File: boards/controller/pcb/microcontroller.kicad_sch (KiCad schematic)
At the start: 23 parts, among them J1001 Conn_01x15_Socket, J1002 Conn_01x11_Socket, J1003 Conn_01x08_Socket, SW1001 SW_Push, SW1002 SW_Push, U1001 STM32U575RITx, X1001 16MHz

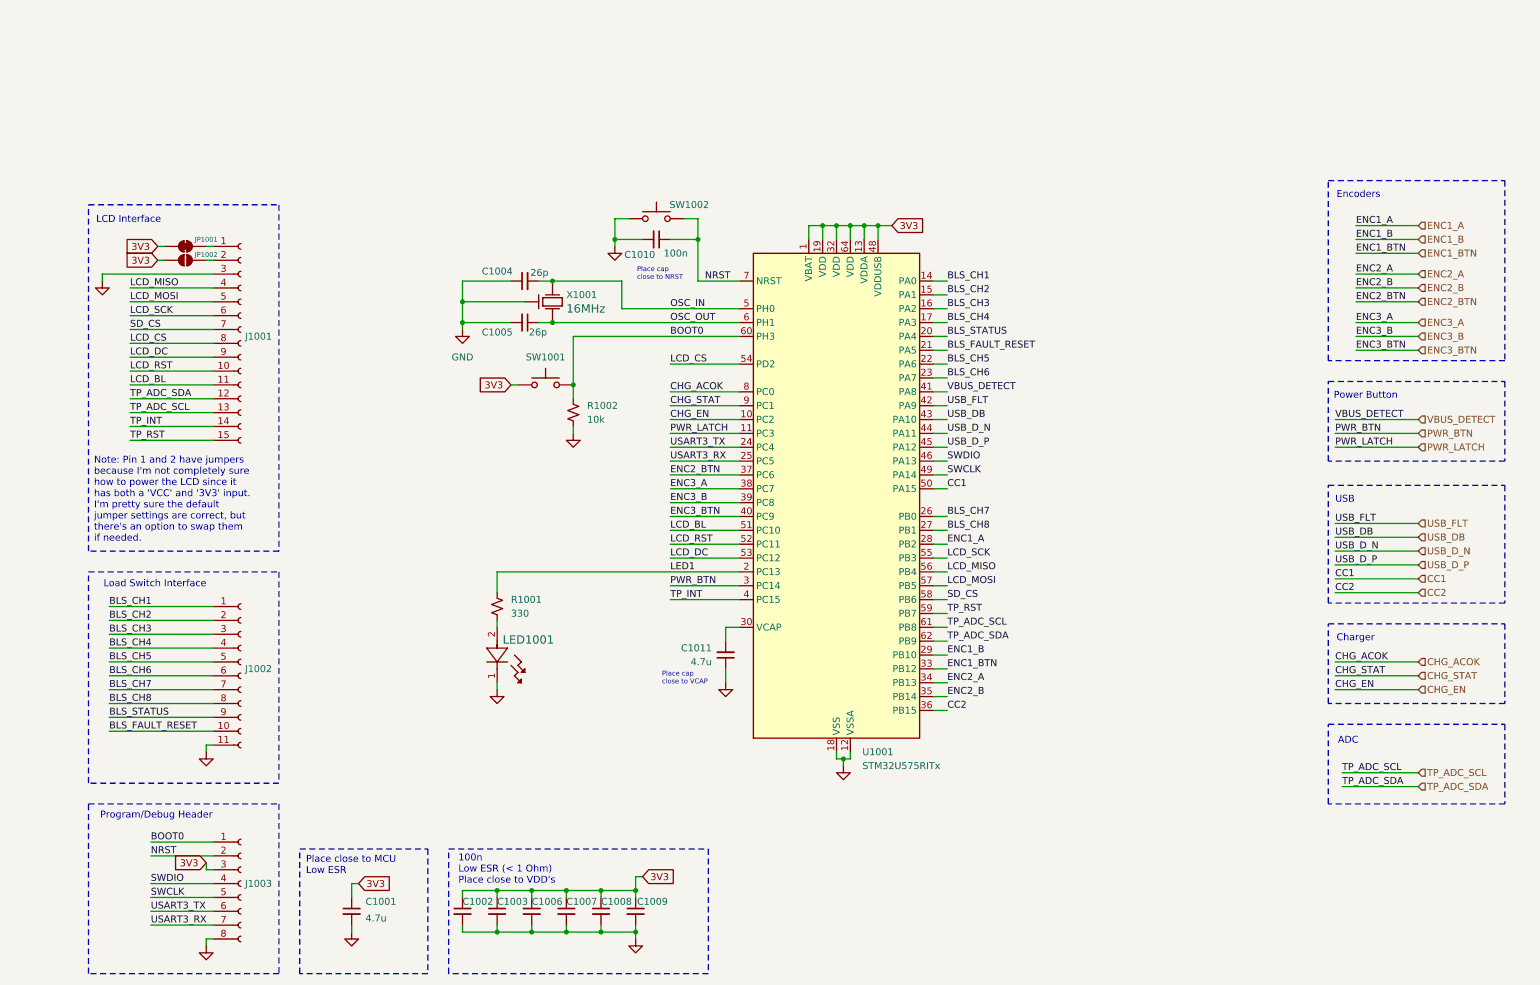
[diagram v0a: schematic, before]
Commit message: controller: pcb: Update schematic
Signed-off-by: Nicholas Loehrke <nicholasnloehrke@gmail.com>
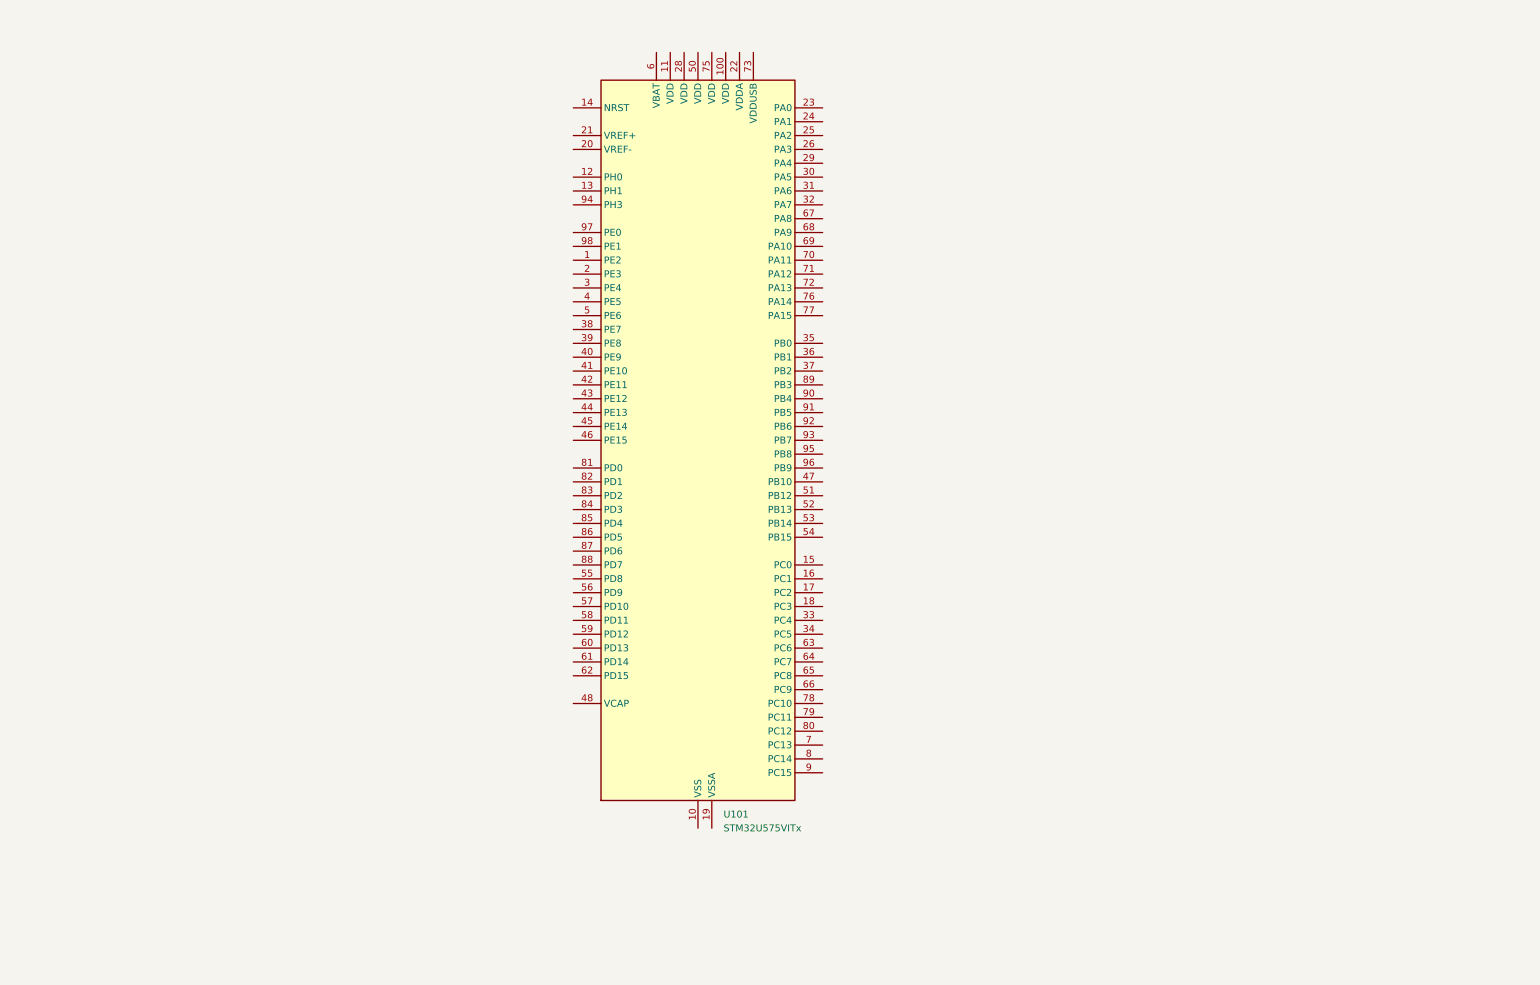
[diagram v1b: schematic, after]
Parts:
- removed C1001, C1011: 4.7u, symbol Device:C_Small
- removed C1002, C1003, C1006, C1007, C1008, C1009, C1010: 100n, symbol Device:C_Small
- removed C1004, C1005: 26p, symbol Device:C_Small
- removed J1001: Conn_01x15_Socket, symbol Connector:Conn_01x15_Socket
- removed J1002: Conn_01x11_Socket, symbol Connector:Conn_01x11_Socket
- removed J1003: Conn_01x08_Socket, symbol Connector:Conn_01x08_Socket
- removed JP1001: SolderJumper_2_Bridged, symbol Jumper:SolderJumper_2_Bridged
- removed JP1002: SolderJumper_2_Open, symbol Jumper:SolderJumper_2_Open
- removed LED1001: B1911PG--20D000514U1930, LED_B1911PG--20D000514U1930_HVK, symbol B1911PG__20D000514U1930:B1911PG--20D000514U1930
- removed R1001: 330, symbol Device:R_Small_US
- removed R1002: 10k, symbol Device:R_Small_US
- removed SW1001, SW1002: SW_Push, symbol Switch:SW_Push
- removed U1001: STM32U575RITx, Package_QFP:LQFP-64_10x10mm_P0.5mm, symbol MCU_ST_STM32U5:STM32U575RITx
- removed X1001: 16MHz, RH100-16.000-18-2030-EXT-TR_RAL, symbol RH100-16.000-18-2030-EXT-TR:RH100-16.000-18-2030-EXT-TR
- added U101: STM32U575VITx, Package_QFP:LQFP-100_14x14mm_P0.5mm, symbol MCU_ST_STM32U5:STM32U575VITx
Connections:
- new net: U101.10 (VSS), U101.27 (VSS), U101.49 (VSS), U101.74 (VSS), U101.99 (VSS)
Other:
- note removed: "100n Low ESR (< 1 Ohm) Place close to VDD's"
- note removed: "ADC"
- note removed: "Charger"
- note removed: "Encoders"
- note removed: "LCD Interface"
- note removed: "Load Switch Interface"
- note removed: "Note: Pin 1 and 2 have jumpers because I'm not completely sure how to power the LCD since it has both a 'VCC' and '3V3' input. I'm pretty sure the default jumper settings are correct, but there's an option to swap them if needed."
- note removed: "Place cap close to NRST"
- note removed: "Place cap close to VCAP"
- note removed: "Place close to MCU Low ESR"
- note removed: "Power Button"
- note removed: "Program/Debug Header"
- note removed: "USB"

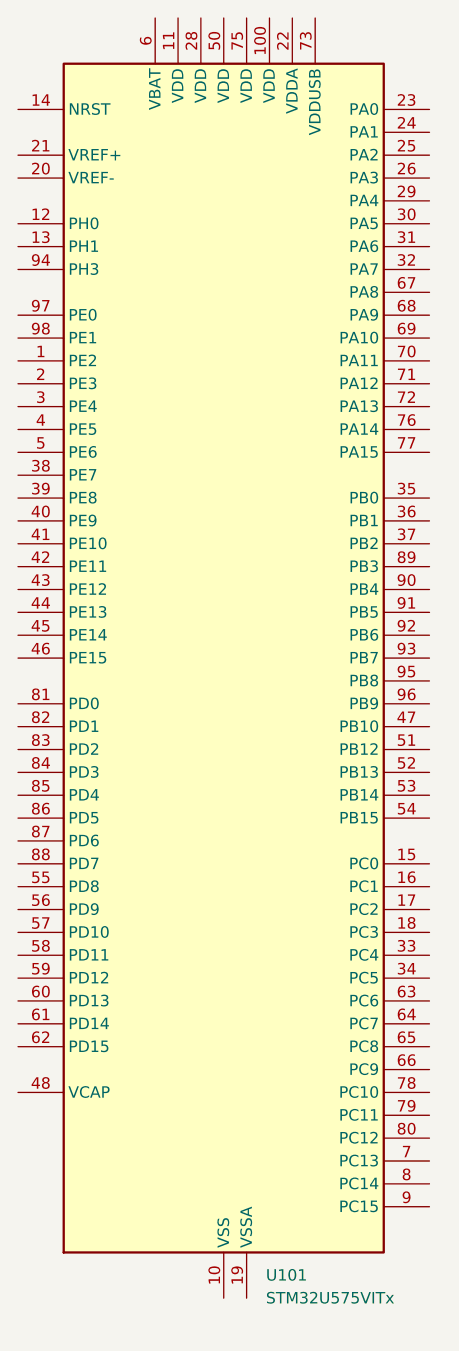
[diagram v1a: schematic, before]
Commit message: controller: pcb: Update schematic
Signed-off-by: Nicholas Loehrke <nicholasnloehrke@gmail.com>
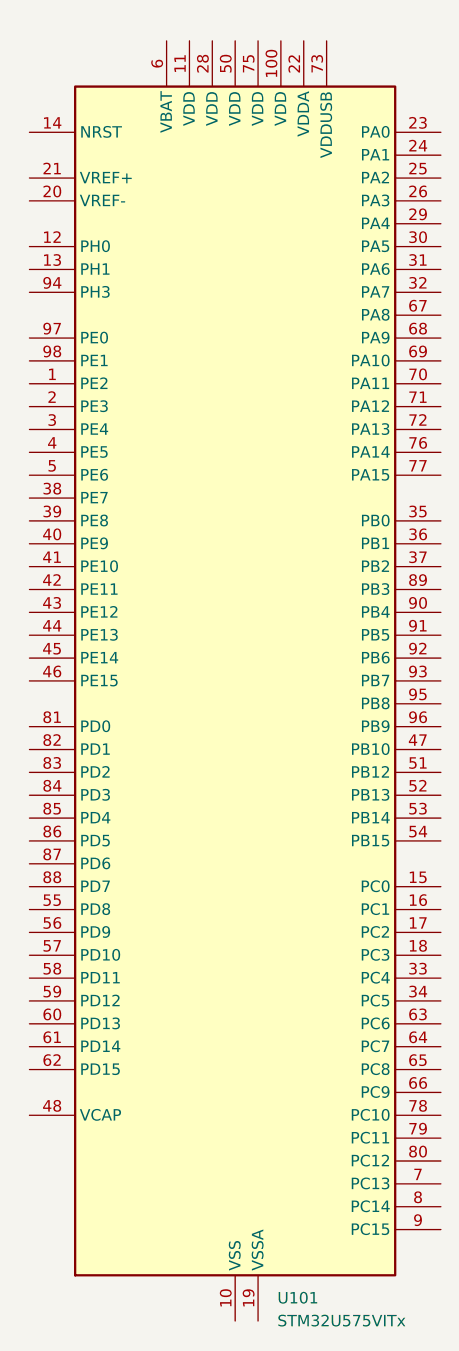
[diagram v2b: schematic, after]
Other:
- moved on the sheet: U101
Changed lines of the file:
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@@
 	(symbol
 		(lib_id "MCU_ST_STM32U5:STM32U575VITx")
-		(at 130.81 92.71 0)
+		(at 132.08 95.25 0)
 		(unit 1)
 		(exclude_from_sim no)
@@
 		(fields_autoplaced yes)
 		(property "Reference" "U101"
-			(at 135.4933 161.29 0)
+			(at 136.7633 163.83 0)
 			(effects
 				(font
@@
 		)
 		(property "Value" "STM32U575VITx"
-			(at 135.4933 163.83 0)
+			(at 136.7633 166.37 0)
 			(effects
 				(font
@@
 		)
 		(property "Footprint" "Package_QFP:LQFP-100_14x14mm_P0.5mm"
-			(at 113.03 158.75 0)
+			(at 114.3 161.29 0)
 			(effects
 				(font
@@
 		)
 		(property "Datasheet" "https://www.st.com/resource/en/datasheet/stm32u575vi.pdf"
-			(at 130.81 92.71 0)
+			(at 132.08 95.25 0)
 			(effects
 				(font
@@
 		)
 		(property "Description" "STMicroelectronics Arm Cortex-M33 MCU, 2048KB flash, 786KB RAM, 160 MHz, 1.71-3.6V, 82 GPIO, LQFP100"
-			(at 130.81 92.71 0)
+			(at 132.08 95.25 0)
 			(effects
 				(font

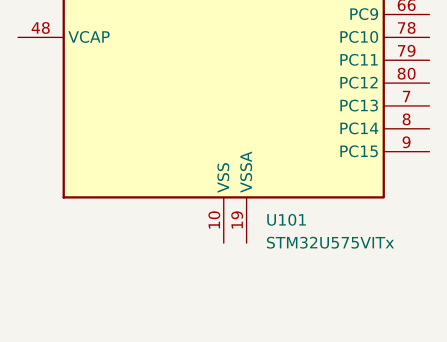
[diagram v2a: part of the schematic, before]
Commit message: controller: pcb: Update schematic
Signed-off-by: Nicholas Loehrke <nicholasnloehrke@gmail.com>
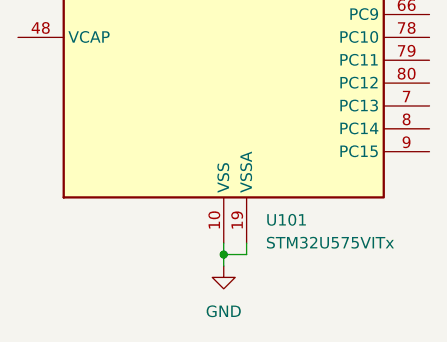
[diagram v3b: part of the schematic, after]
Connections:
- net GND: now reaches U101.10 (VSS), U101.27 (VSS), U101.49 (VSS), U101.74 (VSS), U101.99 (VSS)
- net GND: now also U101.19 (VSSA)
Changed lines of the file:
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@@
 	(generator_version "9.0")
 	(paper "A4")
+	(junction
+		(at 132.08 167.64)
+		(diameter 0)
+		(color 0 0 0 0)
+	)
+	(wire
+		(pts
+			(xy 134.62 166.37) (xy 134.62 167.64)
+		)
+		(stroke
+			(width 0)
+			(type default)
+		)
+	)
+	(wire
+		(pts
+			(xy 132.08 166.37) (xy 132.08 167.64)
+		)
+		(stroke
+			(width 0)
+			(type default)
+		)
+	)
+	(wire
+		(pts
+			(xy 132.08 167.64) (xy 132.08 168.91)
+		)
+		(stroke
+			(width 0)
+			(type default)
+		)
+	)
+	(wire
+		(pts
+			(xy 134.62 167.64) (xy 132.08 167.64)
+		)
+		(stroke
+			(width 0)
+			(type default)
+		)
+	)
 	(symbol
 		(lib_id "MCU_ST_STM32U5:STM32U575VITx")
@@
 					(unit 1)
 				)
+			)
+		)
+	)
+	(symbol
+		(lib_id "power:GND")
+		(at 132.08 168.91 0)
+		(unit 1)
+		(exclude_from_sim no)
+		(in_bom yes)
+		(on_board yes)
+		(dnp no)
+		(fields_autoplaced yes)
+		(property "Reference" "#PWR0301"
+			(at 132.08 175.26 0)
+			(effects
+				(font
+					(size 1.27 1.27)
+				)
+				(hide yes)
+			)
+		)
+		(property "Value" "GND"
+			(at 132.08 173.99 0)
+			(effects
+				(font
+					(size 1.27 1.27)
+				)
+			)
+		)
+		(property "Footprint" ""
+			(at 132.08 168.91 0)
+			(effects
+				(font
+					(size 1.27 1.27)
+				)
+				(hide yes)
+			)
+		)
+		(property "Datasheet" ""
+			(at 132.08 168.91 0)
+			(effects
+				(font
+					(size 1.27 1.27)
+				)
+				(hide yes)
+			)
+		)
+		(property "Description" "Power symbol creates a global label with name \"GND\" , ground"
+			(at 132.08 168.91 0)
+			(effects
+				(font
+					(size 1.27 1.27)
+				)
+				(hide yes)
+			)
+		)
+		(pin "1"
+		)
+		(instances
+			(project ""
+				(path "/5caba13a-97ae-46d4-856f-900b12012fd8/656fb25c-ff6c-44f4-9a62-a4f6fe4240ec"
+					(reference "#PWR0301")
+					(unit 1)
+				)

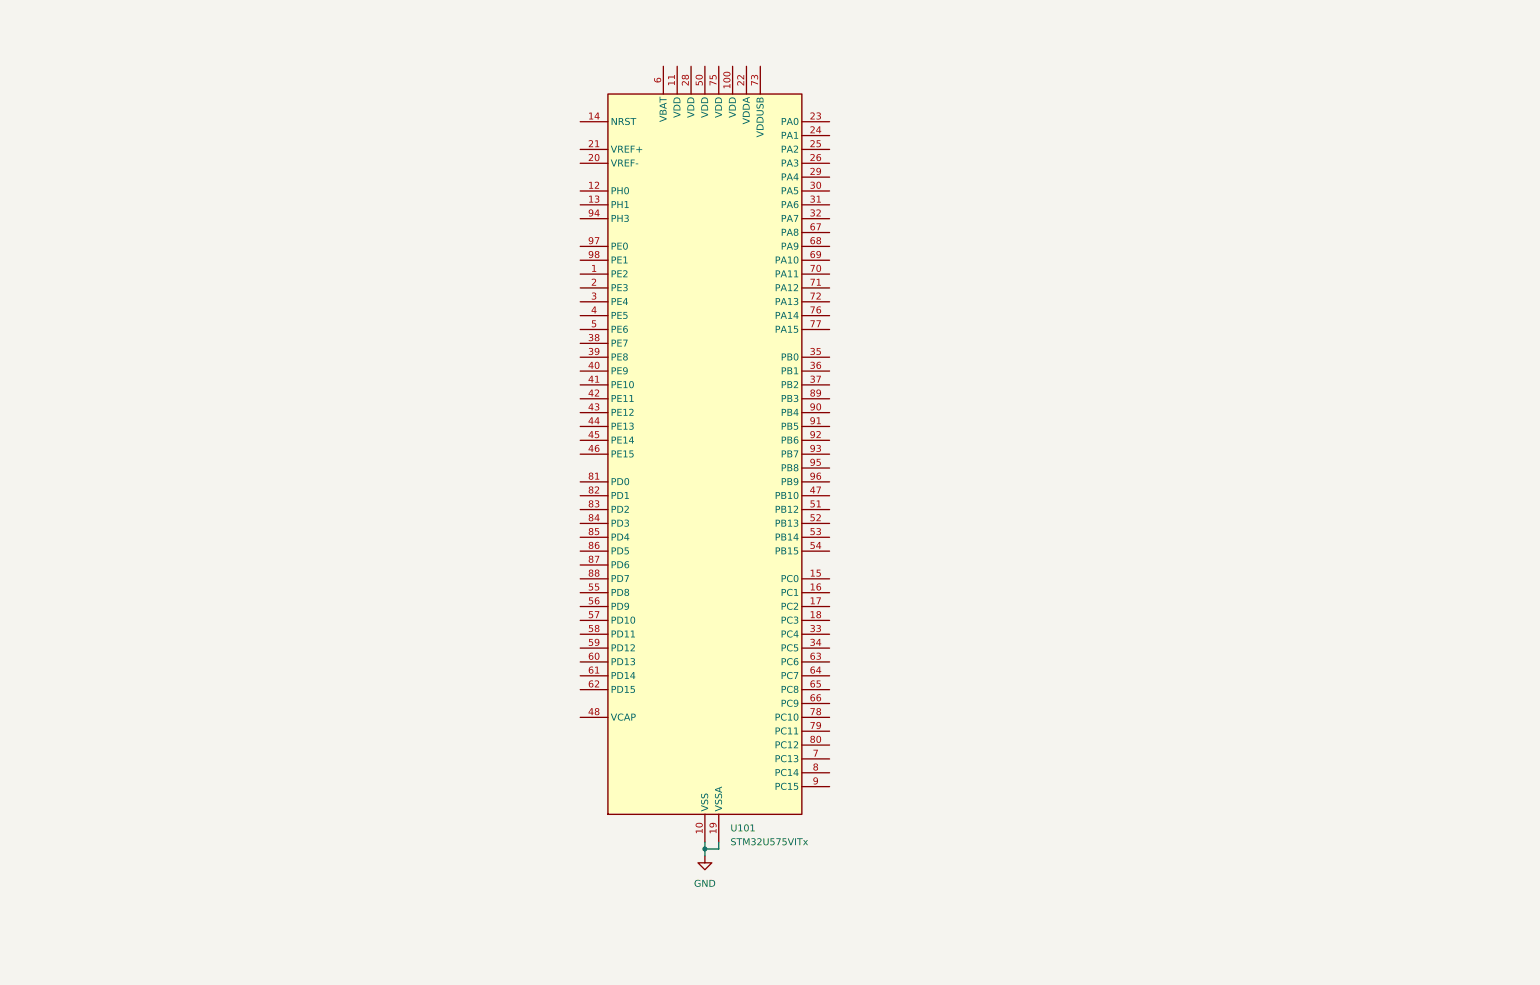
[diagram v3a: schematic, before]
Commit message: controller: pcb: Update schematic
Signed-off-by: Nicholas Loehrke <nicholasnloehrke@gmail.com>
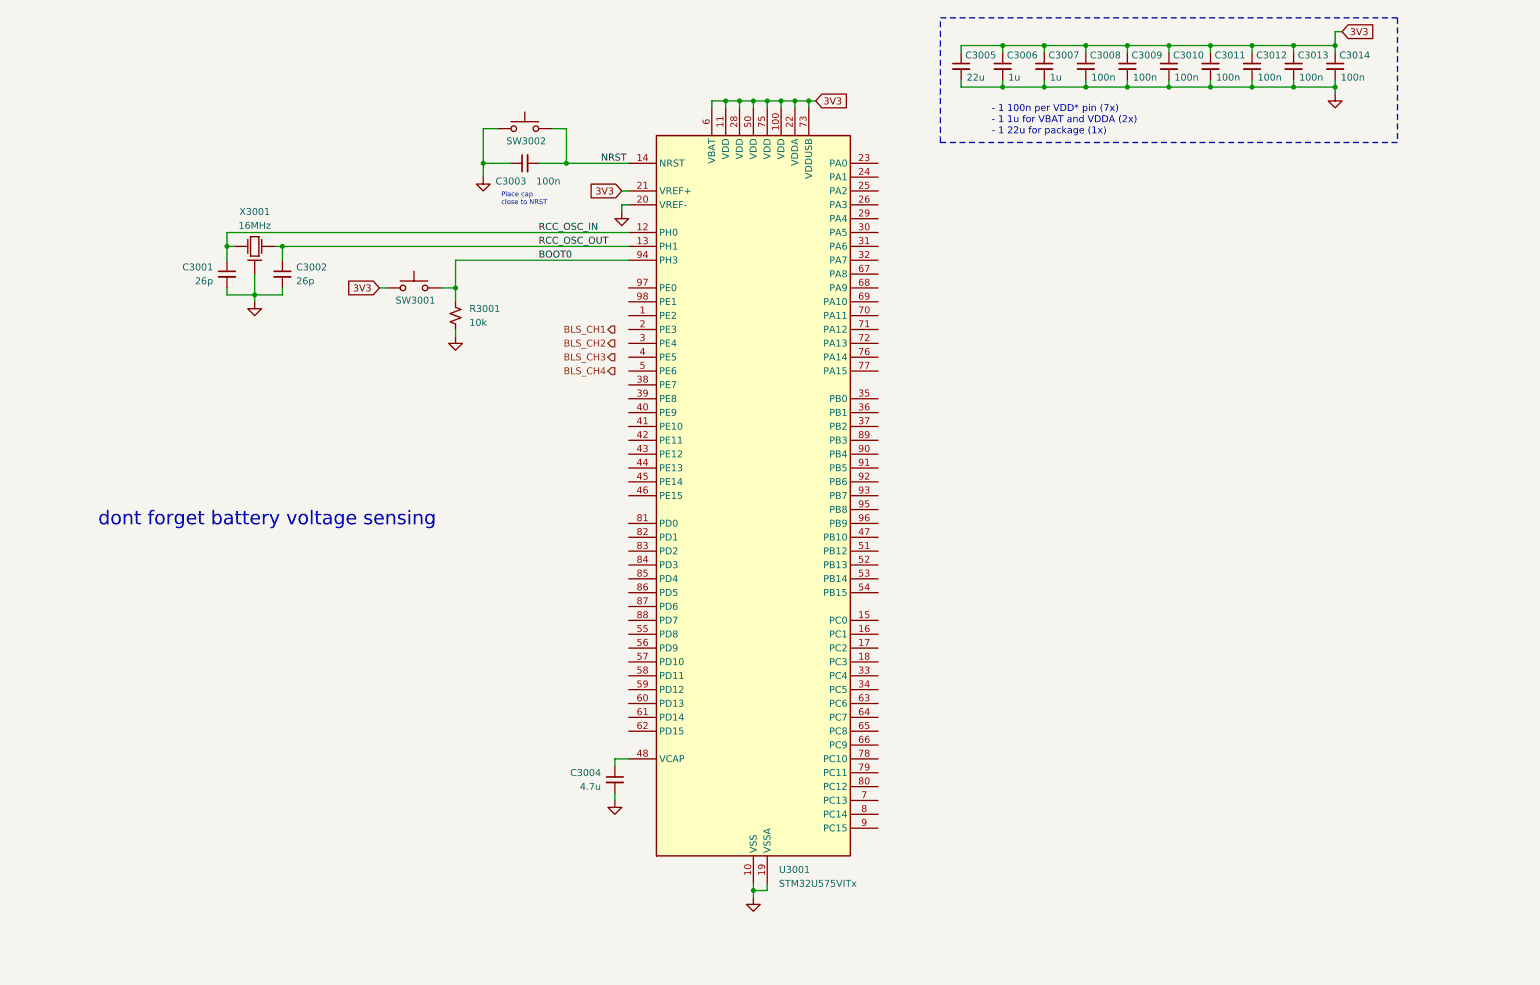
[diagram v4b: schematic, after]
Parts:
- added C3001, C3002: 26p, symbol Device:C_Small
- added C3003, C3008, C3009, C3010, C3011, C3012, C3013, C3014: 100n, symbol Device:C_Small
- added C3004: 4.7u, symbol Device:C_Small
- added C3005: 22u, symbol Device:C_Small
- added C3006, C3007: 1u, symbol Device:C_Small
- added R3001: 10k, symbol Device:R_Small_US
- added SW3001, SW3002: SW_Push, symbol Switch:SW_Push
- added X3001: 16MHz, RH100-16.000-18-2030-EXT-TR_RAL, symbol RH100-16.000-18-2030-EXT-TR:RH100-16.000-18-2030-EXT-TR
- renumbered U101 to U3001
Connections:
- net GND: now also U3001.20 (VREF-), C3001.2, C3002.2, C3003.1, C3004.2, C3005.2, C3006.2, C3007.2, C3008.2, C3009.2, C3010.2, C3011.2, C3012.2, C3013.2, C3014.2, R3001.2, SW3002.1, X3001.2, X3001.4
- net 3V3: now reaches U3001.100 (VDD)
- net 3V3: now also U3001.11 (VDD), U3001.21 (VREF+), U3001.22 (VDDA), U3001.28 (VDD), U3001.50 (VDD), U3001.6 (VBAT), U3001.73 (VDDUSB), U3001.75 (VDD), C3005.1, C3006.1, C3007.1, C3008.1, C3009.1, C3010.1, C3011.1, C3012.1, C3013.1, C3014.1, SW3001.1
- net RCC_OSC_IN: now reaches U3001.12 (PH0)
- net RCC_OSC_IN: now also C3001.1, X3001.1
- net RCC_OSC_OUT: now reaches U3001.13 (PH1)
- net RCC_OSC_OUT: now also C3002.1, X3001.3
- net NRST: now reaches U3001.14 (NRST)
- net NRST: now also C3003.2, SW3002.2
- net at U3001.48 (VCAP): now also C3004.1
- net BOOT0: now reaches U3001.94 (PH3)
- net BOOT0: now also R3001.1, SW3001.2
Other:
- note added: "- 1 100n per VDD* pin (7x) - 1 1u for VBAT and VDDA (2x) - 1 22u for package (1x)"
- note added: "Place cap close to NRST"
- note added: "dont forget battery voltage sensing"
- moved on the sheet: U3001
